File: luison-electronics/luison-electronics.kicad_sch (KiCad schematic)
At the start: 46 parts, among them SW1 EECO_Micro-Dip_3500_B02, SW2 SW_Push, SW3 EECO_Micro-Dip_3500_B02, U1 YAAJ_DCDC_StepDown_LM2596, U2 Robochallenge_KillSwitch

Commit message: asd
asd
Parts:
- removed C1, C2, C4: 100nf, Capacitor_THT:C_Disc_D6.0mm_W2.5mm_P5.00mm, symbol Device:C
- removed C3: C, Capacitor_THT:CP_Radial_D5.0mm_P2.50mm, symbol Device:C
- removed GYRO1: MPU-6050 Breakout Board, keilev_Library:MPU6050 Breakout Board, symbol keilev_Library:MPU-6050 Breakout Board
- removed LS_BL1, LS_BR1, LS_FL1, LS_FR1: Line_Sensor, TerminalBlock:TerminalBlock_bornier-3_P5.08mm, symbol luison-electronics:Line_Sensor
- removed MCU1: ESP32-Node32s, luison-electronics:ESP32-Node32s, symbol luison-electronics:ESP32-Node32s
- removed MD1: H-Bridge_Driver, Connector_PinHeader_2.54mm:PinHeader_2x05_P2.54mm_Vertical, symbol luison-electronics:H-Bridge_Driver
- removed PSFC1, PSFL1, PSFR1, PSL1, PS_B1, PS_R1: Omron_E3Z-D62_2M, TerminalBlock:TerminalBlock_bornier-3_P5.08mm, symbol luison-electronics:Omron_E3Z-D62_2M
- removed Pow1: Power_Supply, TerminalBlock:TerminalBlock_bornier-2_P5.08mm, symbol luison-electronics:Power_Supply
- removed R1, R2, R3, R4, R5, R6: 1Meg, Resistor_THT:R_Axial_DIN0207_L6.3mm_D2.5mm_P7.62mm_Horizontal, symbol Device:R
- removed RC1: Remote_Control_Module, TerminalBlock:TerminalBlock_bornier-2_P5.08mm, symbol luison-electronics:Remote_Control_Module
- removed SW1: EECO_Micro-Dip_3500_B02, luison-electronics:EECO Rotary Switch, symbol luison-electronics:EECO_Micro-Dip_3500_B02
- removed SW2: SW_Push, Button_Switch_THT:SW_PUSH_6mm, symbol Switch:SW_Push
- removed U1: YAAJ_DCDC_StepDown_LM2596, luison-electronics:YAAJ_DCDC_StepDown_LM2596, symbol yaaj_dcdc_stepdown_lm2596:YAAJ_DCDC_StepDown_LM2596
- added PS10: COOLER, luison-electronics:JST_XH_B3B-XH-A_1x03_P2.50mm_Vertical, symbol luison-electronics:Omron_E3Z-D62_2M
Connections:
- net +24V: now also PS10.1 (VCC)
- net GND: now also PS10.3 (GND)
- no-connect marks 14 -> 4

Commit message: asdf
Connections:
- net LS_BR: now also MCU2.26 (IO1/ADC); no longer MCU2.28 (IO42)
- net LS_FR: now also MCU2.25 (IO44); no longer MCU2.24 (IO43)
- net SCL: now also MCU2.28 (IO42); no longer MCU2.26 (IO1/ADC)
- net SDA: now also MCU2.27 (IO2/ADC); no longer MCU2.25 (IO44)
- net SW_P8: now also MCU2.32 (IO38); no longer MCU2.31 (IO39)
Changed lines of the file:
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@@
     (effects (font (size 1.27 1.27)) (justify left bottom))
   )
-  (label "LS_FR" (at 158.75 81.28 0) (fields_autoplaced)
+  (label "LS_FR" (at 158.75 83.82 0) (fields_autoplaced)
     (effects (font (size 1.27 1.27)) (justify left bottom))
   )
@@
     (effects (font (size 1.27 1.27)) (justify left bottom))
   )
-  (label "SW_P8" (at 158.75 99.06 0) (fields_autoplaced)
+  (label "SW_P8" (at 158.75 101.6 0) (fields_autoplaced)
     (effects (font (size 1.27 1.27)) (justify left bottom))
   )
@@
     (effects (font (size 1.27 1.27)) (justify left bottom))
   )
-  (label "LS_BR" (at 158.75 91.44 0) (fields_autoplaced)
+  (label "LS_BR" (at 158.75 86.36 0) (fields_autoplaced)
     (effects (font (size 1.27 1.27)) (justify left bottom))
   )
@@
     (effects (font (size 1.27 1.27)) (justify right bottom))
   )
-  (label "SDA" (at 158.75 83.82 0) (fields_autoplaced)
+  (label "SDA" (at 158.75 88.9 0) (fields_autoplaced)
     (effects (font (size 1.27 1.27)) (justify left bottom))
   )
@@
     (effects (font (size 1.27 1.27)) (justify left bottom))
   )
-  (label "SCL" (at 158.75 86.36 0) (fields_autoplaced)
+  (label "SCL" (at 158.75 91.44 0) (fields_autoplaced)
     (effects (font (size 1.27 1.27)) (justify left bottom))
   )

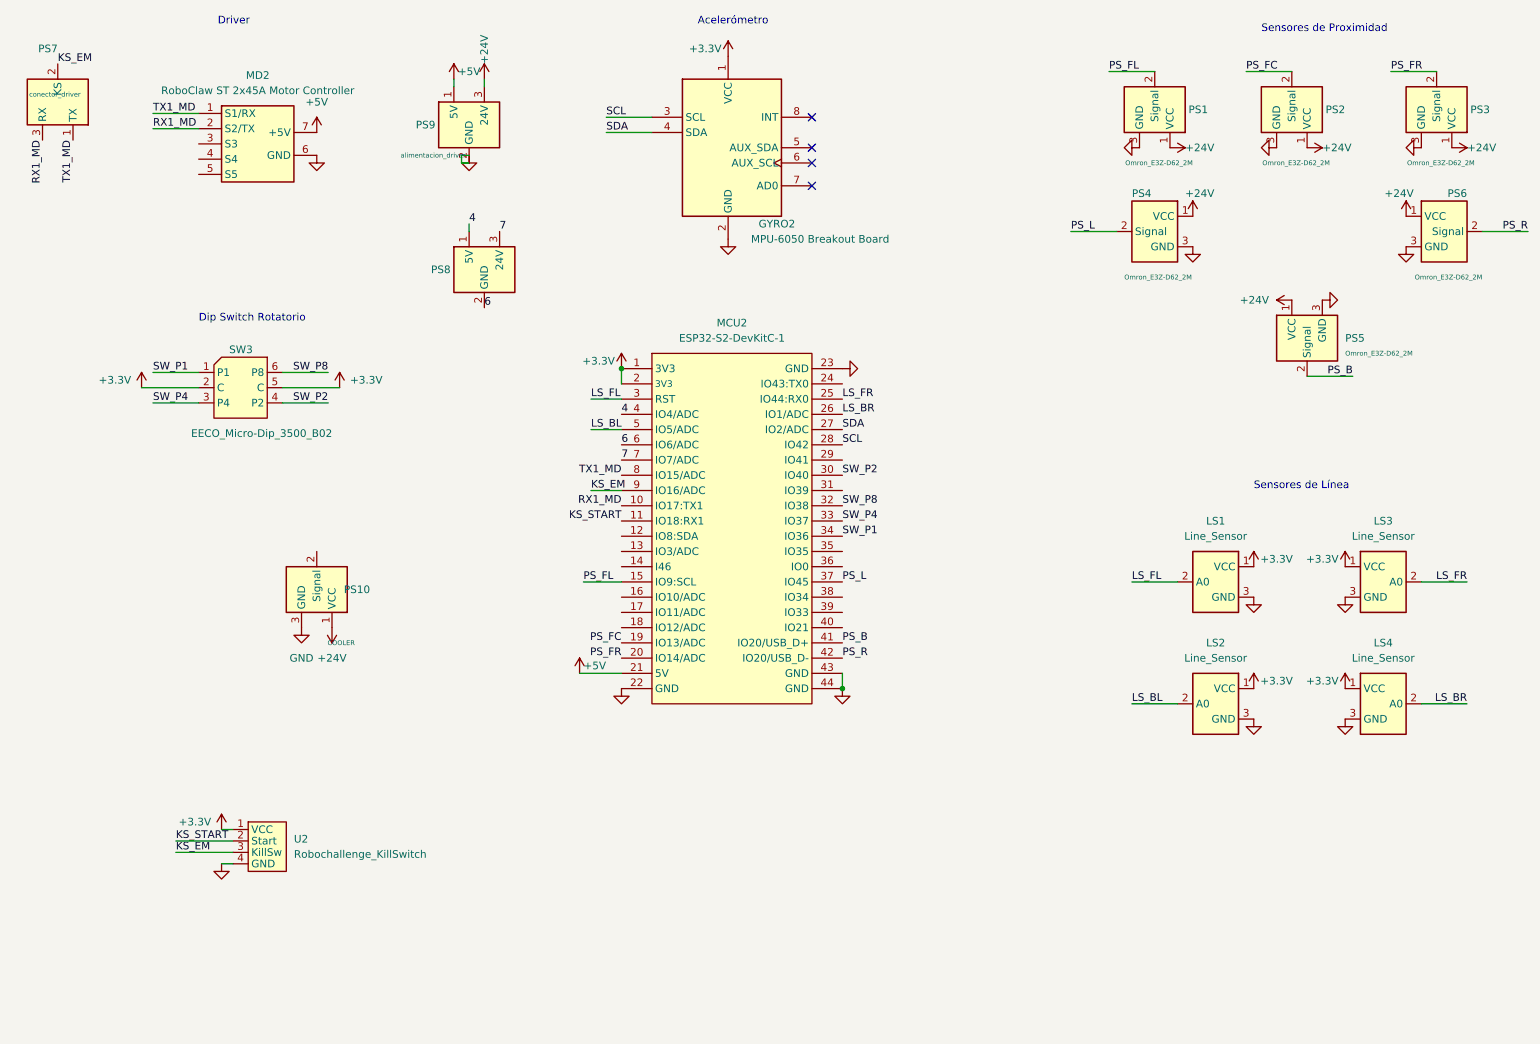
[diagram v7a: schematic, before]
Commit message: Update pcb with correct pins and constraints
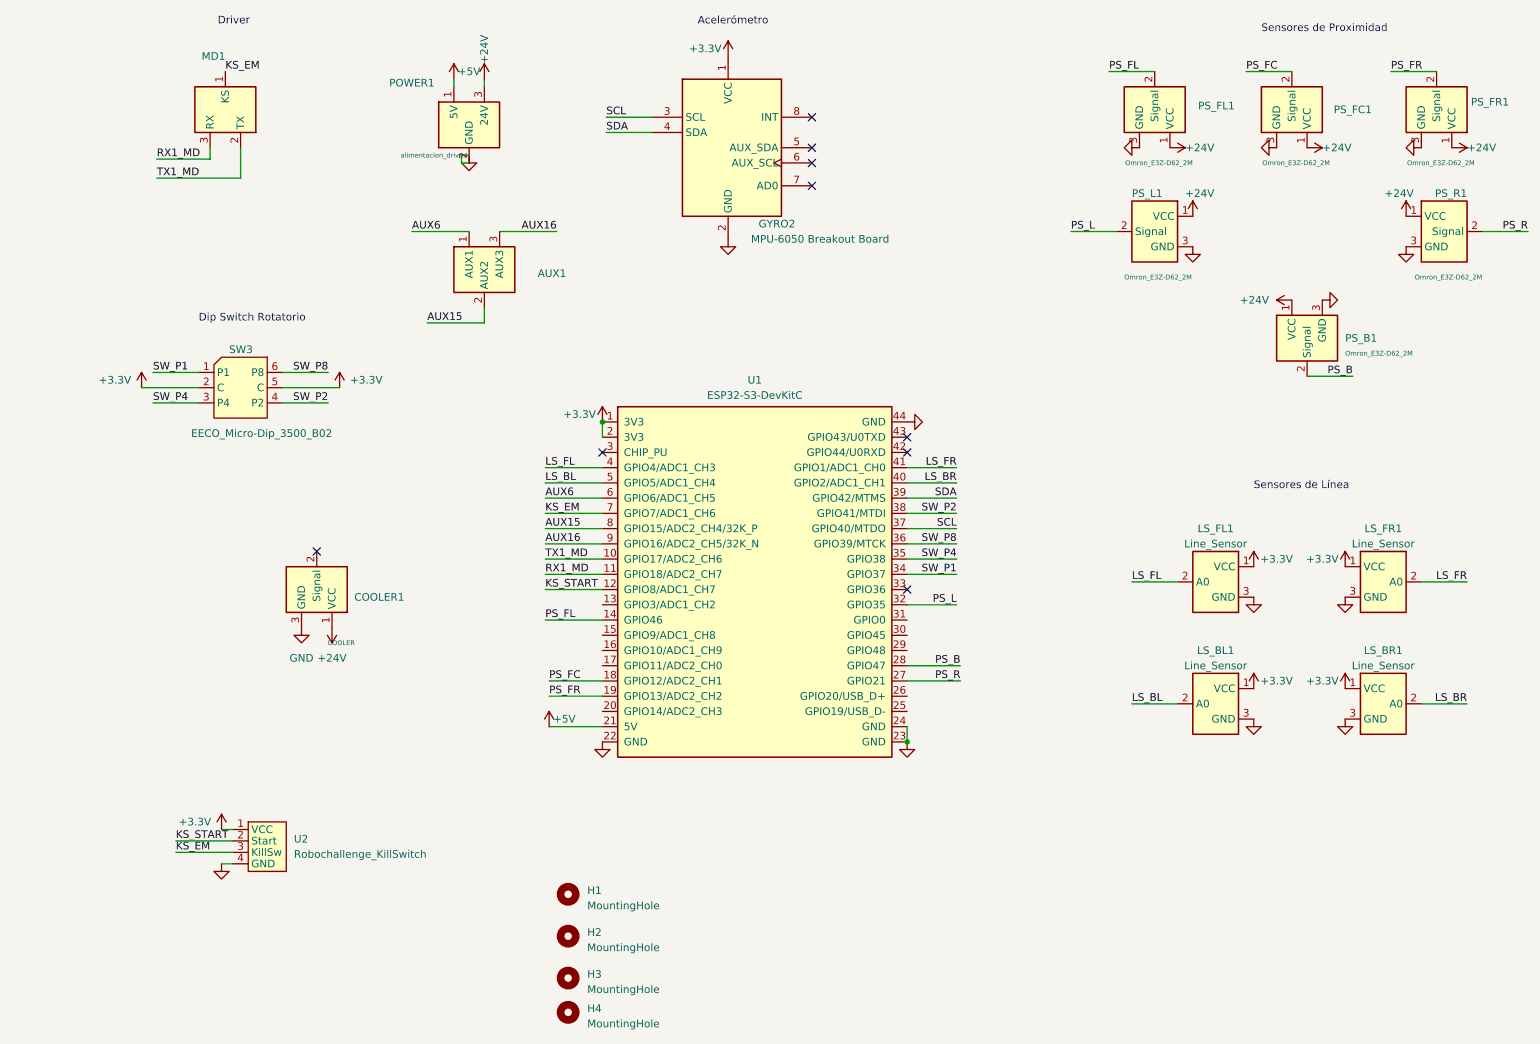
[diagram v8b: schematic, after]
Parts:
- removed MCU2: ESP32-S2-DevKitC-1, luison-electronics:ESP32-S2-DevKitC-1, symbol luison-electronics:ESP32-S2-DevKitC-1
- removed MD2: RoboClaw ST 2x45A Motor Controller, symbol luison-electronics:RoboClaw ST 2x45A Motor Controller
- added H1, H2, H3, H4: MountingHole, MountingHole:MountingHole_3.2mm_M3, symbol Mechanical:MountingHole
- added U1: ESP32-S3-DevKitC, luison-electronics:ESP32-S3-DevKitC, symbol luison-electronics:ESP32-S3-DevKitC
- AUX1: renamed from PS8; value alimentacion_driver -> gpio_aux
- renumbered PS10 to COOLER1, LS2 to LS_BL1, LS4 to LS_BR1, LS1 to LS_FL1, LS3 to LS_FR1, PS7 to MD1, PS9 to POWER1, PS5 to PS_B1, PS2 to PS_FC1, PS1 to PS_FL1, PS3 to PS_FR1, PS4 to PS_L1, PS6 to PS_R1
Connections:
- net +3.3V: now also U1.1 (3V3), U1.2 (3V3)
- net +5V: now also U1.21 (5V)
- net GND: now also U1.22 (GND), U1.23 (GND), U1.24 (GND), U1.44 (GND)
- net KS_EM: now also MD1.1 (KS), U1.7 (GPIO7/ADC1_CH6); no longer MD1.2 (KS)
- net KS_START: now also U1.12 (GPIO8/ADC1_CH7)
- net LS_BL: now also U1.5 (GPIO5/ADC1_CH4)
- net LS_BR: now also U1.40 (GPIO2/ADC1_CH1)
- net LS_FL: now also U1.4 (GPIO4/ADC1_CH3)
- net LS_FR: now also U1.41 (GPIO1/ADC1_CH0)
- net PS_B: now also U1.28 (GPIO47)
- net PS_FC: now also U1.18 (GPIO12/ADC2_CH1)
- net PS_FL: now also U1.14 (GPIO46)
- net PS_FR: now also U1.19 (GPIO13/ADC2_CH2)
- net PS_L: now also U1.32 (GPIO35)
- net PS_R: now also U1.27 (GPIO21)
- net RX1_MD: now also U1.11 (GPIO18/ADC2_CH7)
- net SCL: now also U1.37 (GPIO40/MTDO)
- net SDA: now also U1.39 (GPIO42/MTMS)
- net SW_P1: now also U1.34 (GPIO37)
- net SW_P2: now also U1.38 (GPIO41/MTDI)
- net SW_P4: now also U1.35 (GPIO38)
- net SW_P8: now also U1.36 (GPIO39/MTCK)
- net TX1_MD: now also MD1.2 (TX), U1.10 (GPIO17/ADC2_CH6); no longer MD1.1 (TX)
- net 4 renamed AUX6
- net AUX6: now also U1.6 (GPIO6/ADC1_CH5)
- net 6 renamed AUX15
- net AUX15: now also U1.8 (GPIO15/ADC2_CH4/32K_P)
- net 7 renamed AUX16
- net AUX16: now also U1.9 (GPIO16/ADC2_CH5/32K_N)
- no-connect marks 4 -> 9
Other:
- moved on the sheet: MD1
